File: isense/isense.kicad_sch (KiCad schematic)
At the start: 17 parts, among them Q101 NPN, Q102 FMMT597TA, Q103 NMOS, U101 ${SIM.PARAMS}

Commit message: Misc schematic update
Add a few graphical stuff to improve readability
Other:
- note added: "Load simulation"
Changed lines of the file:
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@@
+		)
+	)
+	(rectangle
+		(start 170.18 46.99)
+		(end 254 90.17)
+		(stroke
+			(width 0)
+			(type default)
+		)
+		(fill
+			(type none)
 		)
 	)
@@
 		(effects
 			(font
+				(size 1.27 1.27)
+			)
+		)
+	)
+	(text "Load simulation"
+		(exclude_from_sim no)
+		(at 215.9 50.8 0)
+		(effects
+			(font

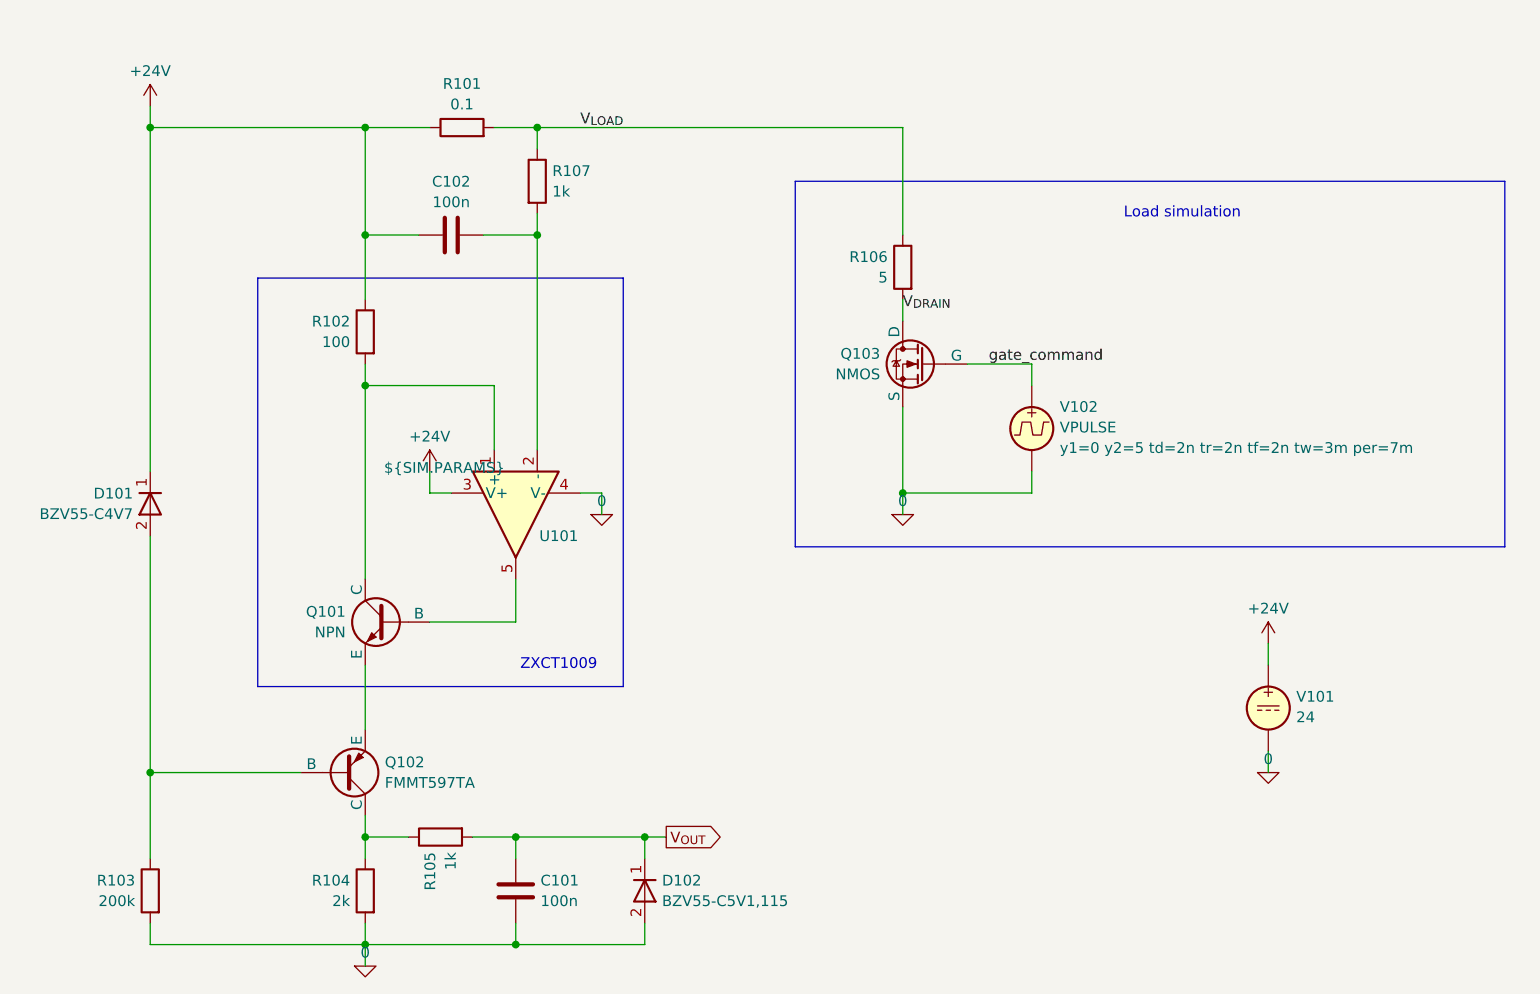
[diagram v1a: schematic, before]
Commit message: Update Simulation model for PNP transistor
* Add Spice models for FMMT597 PNP transistor and ZXCT1009 from Diode Inc. to
  reporsitory.
* Update FMMT597 PNP transistor simulation model.
* Re-run simulation and update parameters
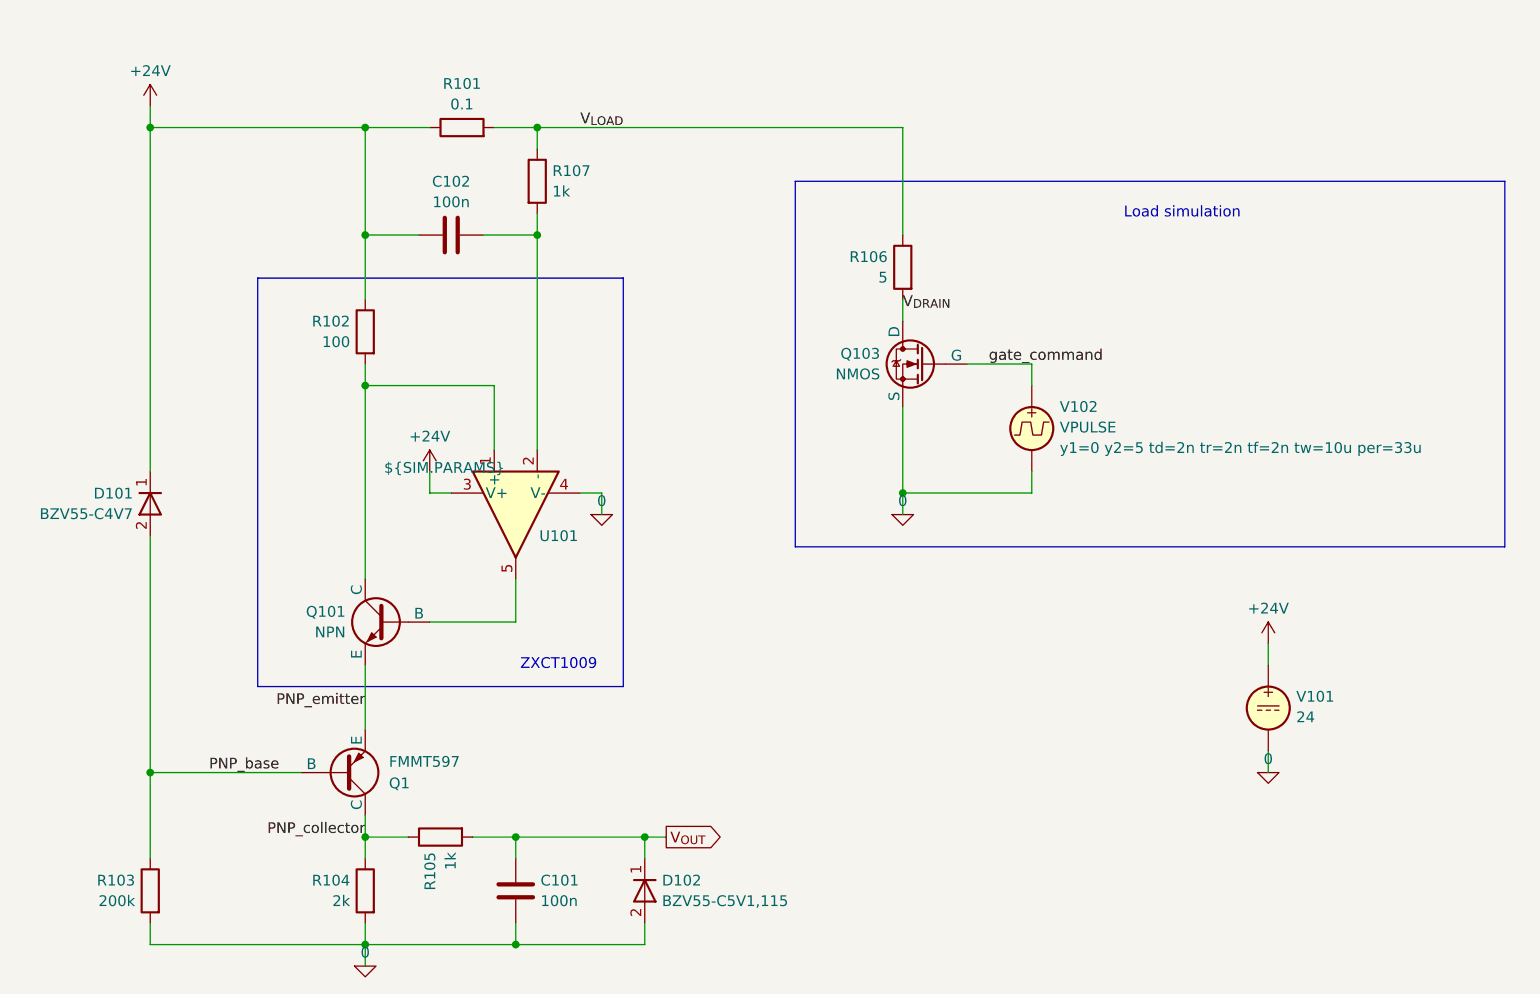
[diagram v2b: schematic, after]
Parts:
- removed Q102: FMMT597TA, symbol Simulation_SPICE:PNP
- added Q1: FMMT597, symbol Simulation_SPICE:PNP
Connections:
- net PNP_collector: now reaches R104.1, R105.1
- net PNP_collector: now also Q1.1 (C)
- net PNP_emitter: now reaches Q101.3 (E)
- net PNP_emitter: now also Q1.3 (E)
- net PNP_base: now reaches D101.2 (A), R103.1
- net PNP_base: now also Q1.2 (B)
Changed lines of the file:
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@@
+		)
+	)
+	(label "PNP_emitter"
+		(at 119.38 109.22 180)
+		(effects
+			(font
+				(size 1.25 1.25)
+			)
+			(justify right bottom)
+		)
+	)
+	(label "PNP_base"
+		(at 109.22 116.84 180)
+		(effects
+			(font
+				(size 1.25 1.25)
+			)
+			(justify right bottom)
 		)
 	)
@@
 			)
 			(justify left bottom)
+		)
+	)
+	(label "PNP_collector"
+		(at 119.38 124.46 180)
+		(effects
+			(font
+				(size 1.25 1.25)
+			)
+			(justify right bottom)
 		)
 	)
@@
 			)
 		)
-		(property "Sim.Params" "y1=0 y2=5 td=2n tr=2n tf=2n tw=3m per=7m"
+		(property "Sim.Params" "y1=0 y2=5 td=2n tr=2n tf=2n tw=10u per=33u"
 			(at 201.422 78.4945 0)
 			(effects
@@
 			)
 		)
-		(property "Sim.Params" "rs=500m cjo=300p"
+		(property "Sim.Params" "rs=500m cjo=300p bv=4.7 ibv=5m fv_max=40 id_max=250m"
 			(at 93.98 85.09 0)
 			(effects
@@
 	)
 	(symbol
+		(lib_id "Simulation_SPICE:D")
+		(at 152.4 130.81 270)
+		(unit 1)
+		(exclude_from_sim no)
+		(in_bom yes)
+		(on_board yes)
+		(dnp no)
+		(property "Reference" "D102"
+			(at 154.432 129.5978 90)
+			(effects
+				(font
+					(size 1.27 1.27)
+				)
+				(justify left)
+			)
+		)
+		(property "Value" "BZV55-C5V1,115"
+			(at 154.432 132.0221 90)
+			(effects
+				(font
+					(size 1.27 1.27)
+				)
+				(justify left)
+			)
+		)
+		(property "Footprint" ""
+			(at 152.4 130.81 0)
+			(effects
+				(font
+					(size 1.27 1.27)
+				)
+				(hide yes)
+			)
+		)
+		(property "Datasheet" "https://ngspice.sourceforge.io/docs/ngspice-html-manual/manual.xhtml#cha_DIODEs"
+			(at 152.4 130.81 0)
+			(effects
+				(font
+					(size 1.27 1.27)
+				)
+				(hide yes)
+			)
+		)
+		(property "Description" "Diode for simulation or PCB"
+			(at 152.4 130.81 0)
+			(effects
+				(font
+					(size 1.27 1.27)
+				)
+				(hide yes)
+			)
+		)
+		(property "Sim.Device" "D"
+			(at 152.4 130.81 0)
+			(effects
+				(font
+					(size 1.27 1.27)
+				)
+				(hide yes)
+			)
+		)
+		(property "Sim.Pins" "1=K 2=A"
+			(at 152.4 130.81 0)
+			(effects
+				(font
+					(size 1.27 1.27)
+				)
+				(hide yes)
+			)
+		)
+		(property "Sim.Params" "rs=480m cjo=300p bv=5.1 ibv=5 fv_max=40 id_max=250m"
+			(at 152.4 130.81 0)
+			(effects
+				(font
+					(size 1.27 1.27)
+				)
+				(hide yes)
+			)
+		)
+		(pin "1"
+		)
+		(pin "2"
+		)
+		(instances
+			(project "isense"
+				(path "/d002ebf6-1637-4164-b68c-36870675b076"
+					(reference "D102")
+					(unit 1)
+				)
+			)
+		)
+	)
+	(symbol
 		(lib_id "Simulation_SPICE:PNP")
 		(at 116.84 116.84 0)
@@
 		(on_board yes)
 		(dnp no)
-		(property "Reference" "Q102"
-			(at 121.6914 115.6278 0)
-			(effects
-				(font
-					(size 1.27 1.27)
-				)
-				(justify left)
-			)
-		)
-		(property "Value" "FMMT597TA"
-			(at 121.6914 118.0521 0)
+		(property "Reference" "Q1"
+			(at 122.174 118.1101 0)
+			(effects
+				(font
+					(size 1.27 1.27)
+				)
+				(justify left)
+			)
+		)
+		(property "Value" "FMMT597"
+			(at 122.174 115.5701 0)
 			(effects
 				(font
@@
 			)
 		)
-		(pin "1"
+		(property "Sim.Library" "FMMT597.spice.lib"
+			(at 116.84 116.84 0)
+			(effects
+				(font
+					(size 1.27 1.27)
+				)
+				(hide yes)
+			)
+		)
+		(property "Sim.Name" "FMMT597"
+			(at 116.84 116.84 0)
+			(effects
+				(font
+					(size 1.27 1.27)
+				)
+				(hide yes)
+			)
 		)
 		(pin "2"
@@
 		(pin "3"
 		)
+		(pin "1"
+		)
 		(instances
 			(project ""
 				(path "/d002ebf6-1637-4164-b68c-36870675b076"
-					(reference "Q102")
-					(unit 1)
-				)
-			)
-		)
-	)
-	(symbol
-		(lib_id "Simulation_SPICE:D")
-		(at 152.4 130.81 270)
-		(unit 1)
-		(exclude_from_sim no)
-		(in_bom yes)
-		(on_board yes)
-		(dnp no)
-		(property "Reference" "D102"
-			(at 154.432 129.5978 90)
-			(effects
-				(font
-					(size 1.27 1.27)
-				)
-				(justify left)
-			)
-		)
-		(property "Value" "BZV55-C5V1,115"
-			(at 154.432 132.0221 90)
-			(effects
-				(font
-					(size 1.27 1.27)
-				)
-				(justify left)
-			)
-		)
-		(property "Footprint" ""
-			(at 152.4 130.81 0)
-			(effects
-				(font
-					(size 1.27 1.27)
-				)
-				(hide yes)
-			)
-		)
-		(property "Datasheet" "https://ngspice.sourceforge.io/docs/ngspice-html-manual/manual.xhtml#cha_DIODEs"
-			(at 152.4 130.81 0)
-			(effects
-				(font
-					(size 1.27 1.27)
-				)
-				(hide yes)
-			)
-		)
-		(property "Description" "Diode for simulation or PCB"
-			(at 152.4 130.81 0)
-			(effects
-				(font
-					(size 1.27 1.27)
-				)
-				(hide yes)
-			)
-		)
-		(property "Sim.Device" "D"
-			(at 152.4 130.81 0)
-			(effects
-				(font
-					(size 1.27 1.27)
-				)
-				(hide yes)
-			)
-		)
-		(property "Sim.Pins" "1=K 2=A"
-			(at 152.4 130.81 0)
-			(effects
-				(font
-					(size 1.27 1.27)
-				)
-				(hide yes)
-			)
-		)
-		(property "Sim.Params" "rs=480m cjo=300p"
-			(at 152.4 130.81 0)
-			(effects
-				(font
-					(size 1.27 1.27)
-				)
-				(hide yes)
-			)
-		)
-		(pin "1"
-		)
-		(pin "2"
-		)
-		(instances
-			(project "isense"
-				(path "/d002ebf6-1637-4164-b68c-36870675b076"
-					(reference "D102")
-					(unit 1)
-				)
+					(reference "Q1")
+					(unit 1)
+				)

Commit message: Update simulation design with ZXCT1009 PSPICE model
* Create `lib/` directory in which to store local libraries
* Create symbol for ZXCT1009
* Update ZXCT1009.spice model so KiCAd accepts it and link it to KiCad symbol
* Update schematic according to directory updates and with new component
* Re-run simulation : doesn't work for now ("x_x)
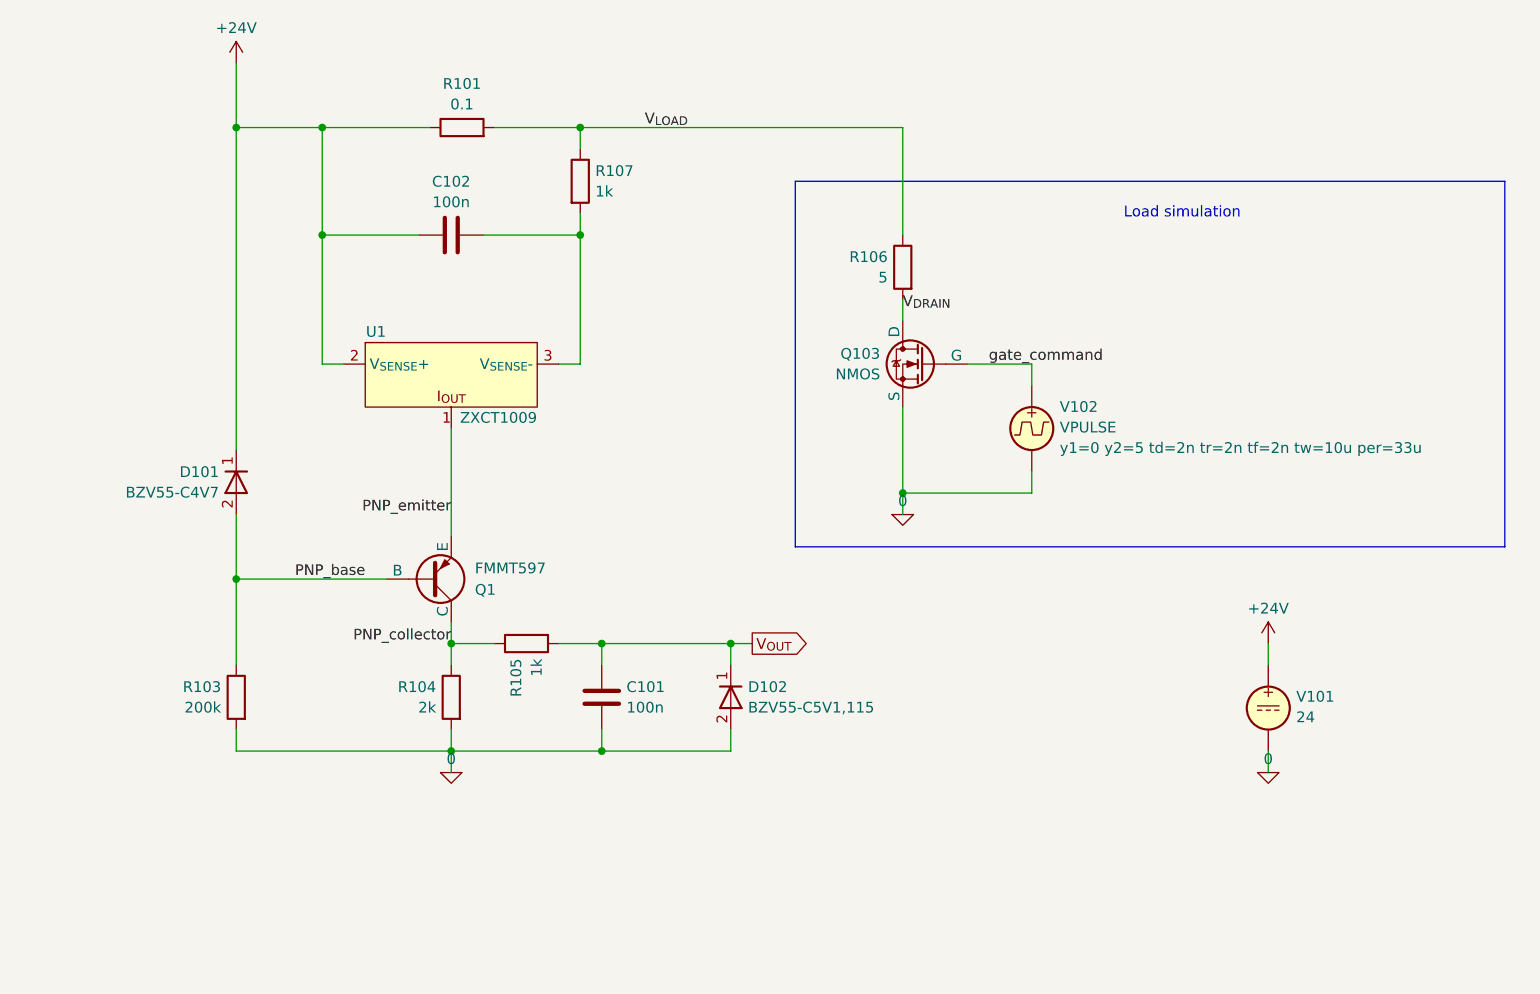
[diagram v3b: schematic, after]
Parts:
- removed Q101: NPN, symbol Simulation_SPICE:NPN
- removed R102: 100, symbol Device:R
- removed U101: ${SIM.PARAMS}, symbol Simulation_SPICE:OPAMP
- added U1: ZXCT1009, symbol ZXCT1009:ZXCT1009
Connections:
- net +24V: now also U1.2 (V_{SENSE}+)
- net PNP_emitter: now also U1.1 (I_{OUT})
- net at C102.2, R107.2: now also U1.3 (V_{SENSE}-)
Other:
- note removed: "ZXCT1009"
- moved on the sheet: C101, D101, D102, Q1, R103, R104, R105, R107
